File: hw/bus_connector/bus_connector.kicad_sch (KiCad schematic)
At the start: 11 parts, among them J1 DB9_Top, J2 DB9_Left, J3 DB9_Right

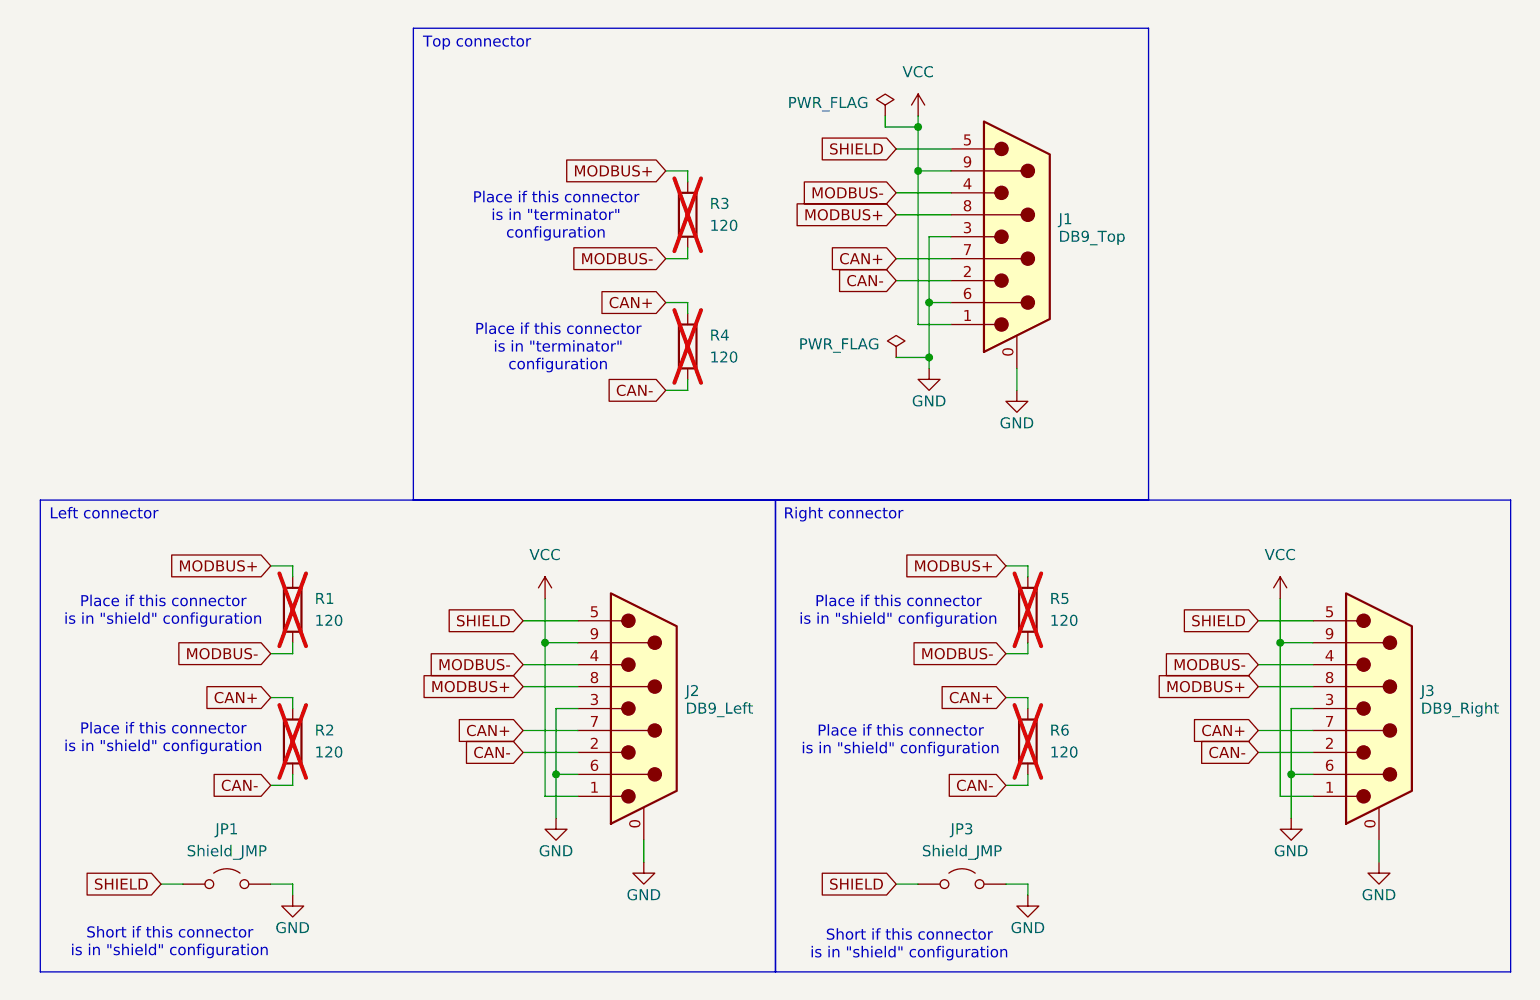
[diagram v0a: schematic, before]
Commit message: Add test layout to connector PCB
Signed-off-by: Mateusz Pająk <22417805+Tai-Min@users.noreply.github.com>
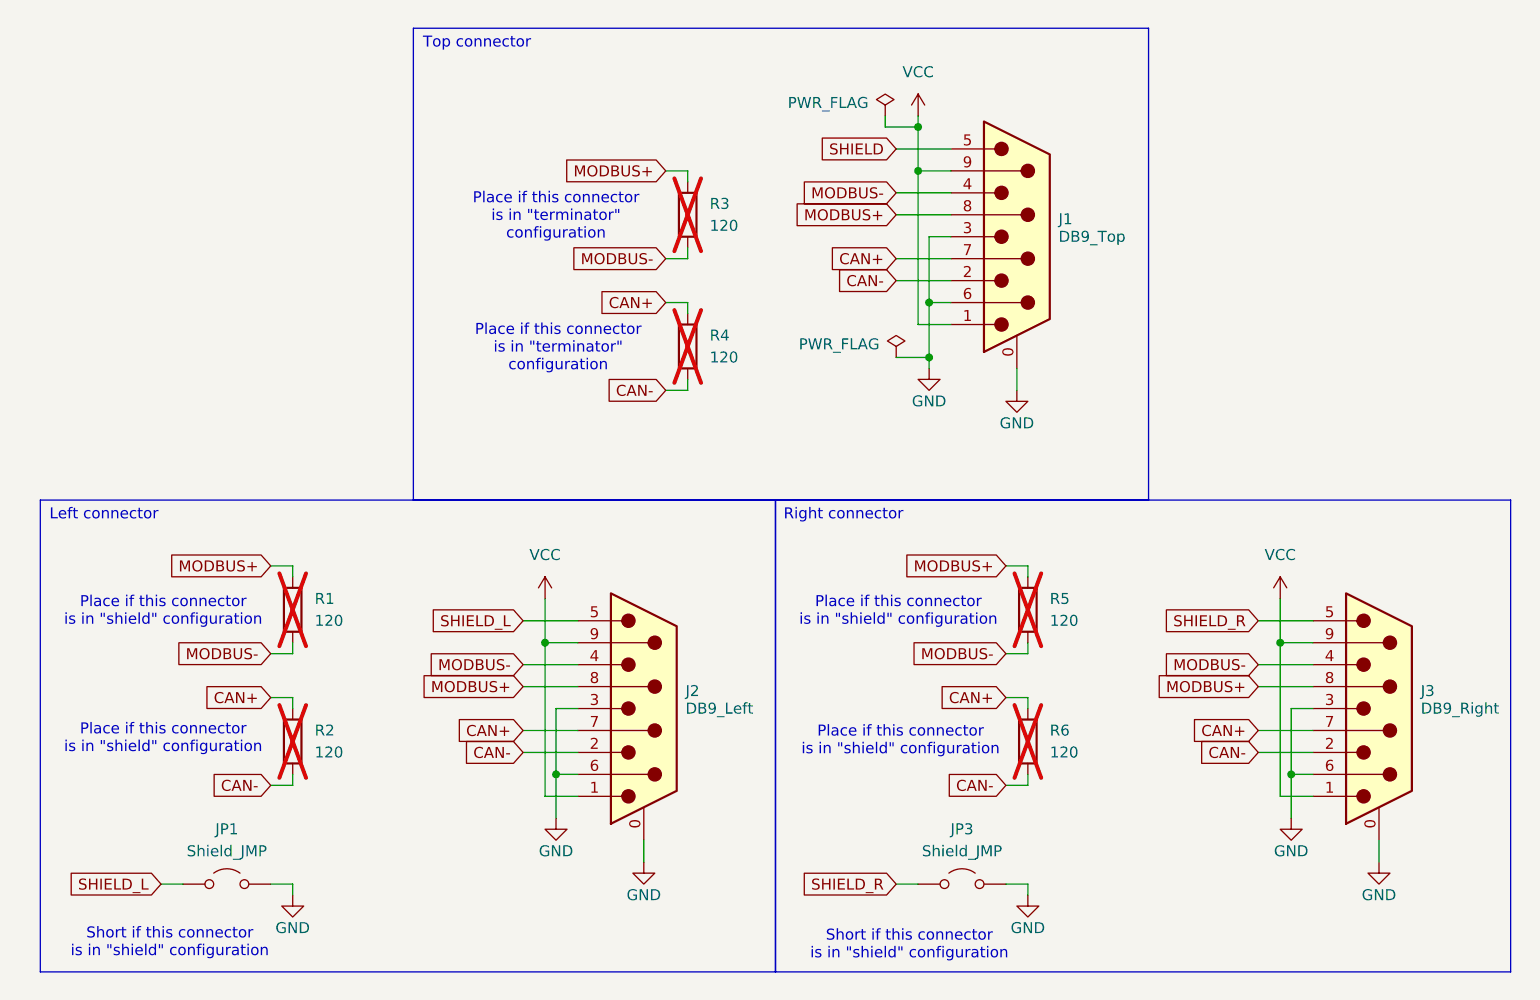
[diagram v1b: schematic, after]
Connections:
- net SHIELD: no longer J2.5, J3.5, JP1.1 (A), JP3.1 (A)
- new net SHIELD_L: J2.5, JP1.1 (A)
- new net SHIELD_R: J3.5, JP3.1 (A)
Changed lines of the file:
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@@
+		)
+	)
+	(global_label "SHIELD_R"
+		(shape input)
+		(at 205.74 104.14 180)
+		(fields_autoplaced yes)
+		(effects
+			(font
+				(size 1.27 1.27)
+			)
+			(justify right)
+		)
+		(property "Intersheetrefs" "${INTERSHEET_REFS}"
+			(at 193.9253 104.14 0)
+			(effects
+				(font
+					(size 1.27 1.27)
+				)
+				(justify right)
+				(hide yes)
+			)
+		)
+	)
+	(global_label "MODBUS-"
+		(shape input)
+		(at 205.74 109.22 180)
+		(fields_autoplaced yes)
+		(effects
+			(font
+				(size 1.27 1.27)
+			)
+			(justify right)
+		)
+		(property "Intersheetrefs" "${INTERSHEET_REFS}"
+			(at 193.3205 109.22 0)
+			(effects
+				(font
+					(size 1.27 1.27)
+				)
+				(justify right)
+				(hide yes)
+			)
 		)
 	)
 	(global_label "SHIELD"
 		(shape input)
-		(at 205.74 104.14 180)
-		(fields_autoplaced yes)
-		(effects
-			(font
-				(size 1.27 1.27)
-			)
-			(justify right)
-		)
-		(property "Intersheetrefs" "${INTERSHEET_REFS}"
-			(at 196.1629 104.14 0)
-			(effects
-				(font
-					(size 1.27 1.27)
-				)
-				(justify right)
-				(hide yes)
-			)
-		)
-	)
-	(global_label "MODBUS-"
-		(shape input)
-		(at 205.74 109.22 180)
-		(fields_autoplaced yes)
-		(effects
-			(font
-				(size 1.27 1.27)
-			)
-			(justify right)
-		)
-		(property "Intersheetrefs" "${INTERSHEET_REFS}"
-			(at 193.3205 109.22 0)
-			(effects
-				(font
-					(size 1.27 1.27)
-				)
-				(justify right)
-				(hide yes)
-			)
-		)
-	)
-	(global_label "SHIELD"
-		(shape input)
 		(at 163.83 49.53 180)
 		(fields_autoplaced yes)
@@
 		)
 	)
-	(global_label "SHIELD"
+	(global_label "SHIELD_R"
 		(shape input)
 		(at 163.83 134.62 180)
@@
 		)
 		(property "Intersheetrefs" "${INTERSHEET_REFS}"
-			(at 154.2529 134.62 0)
+			(at 152.0153 134.62 0)
 			(effects
 				(font
@@
 		)
 	)
-	(global_label "SHIELD"
+	(global_label "SHIELD_L"
 		(shape input)
 		(at 120.65 104.14 180)
@@
 		)
 		(property "Intersheetrefs" "${INTERSHEET_REFS}"
-			(at 111.0729 104.14 0)
+			(at 109.0772 104.14 0)
 			(effects
 				(font
@@
 		)
 	)
-	(global_label "SHIELD"
+	(global_label "SHIELD_L"
 		(shape input)
 		(at 78.74 134.62 180)
@@
 		)
 		(property "Intersheetrefs" "${INTERSHEET_REFS}"
-			(at 69.1629 134.62 0)
-			(effects
-				(font
+			(at 67.1672 134.62 0)
+			(effects
+				(font

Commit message: Edit actions
Signed-off-by: Mateusz Pająk <22417805+Tai-Min@users.noreply.github.com>
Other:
- moved on the sheet: J1, J2, J3, JP1, JP3, R1, R2, R3, R4, R5, R6

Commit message: Fix issues with bus connector project
Signed-off-by: Mateusz Pająk <22417805+Tai-Min@users.noreply.github.com>
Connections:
- net SHIELD: no longer names the net of J1.5
- no-connect marks 0 -> 1
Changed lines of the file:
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@@
 		(color 0 0 0 0)
 	)
+	(no_connect
+		(at 170.18 50.8)
+	)
 	(wire
 		(pts
@@
 		(pts
 			(xy 139.7 68.58) (xy 137.16 68.58)
-		)
-		(stroke
-			(width 0)
-			(type default)
-		)
-	)
-	(wire
-		(pts
-			(xy 163.83 50.8) (xy 170.18 50.8)
 		)
 		(stroke
@@
 			(effects
 				(font
-					(size 1.27 1.27)
-				)
-				(justify right)
-				(hide yes)
-			)
-		)
-	)
-	(global_label "SHIELD"
-		(shape input)
-		(at 163.83 50.8 180)
-		(fields_autoplaced yes)
-		(effects
-			(font
-				(size 1.27 1.27)
-			)
-			(justify right)
-		)
-		(property "Intersheetrefs" "${INTERSHEET_REFS}"
-			(at 154.2529 50.8 0)
-			(effects
-				(font

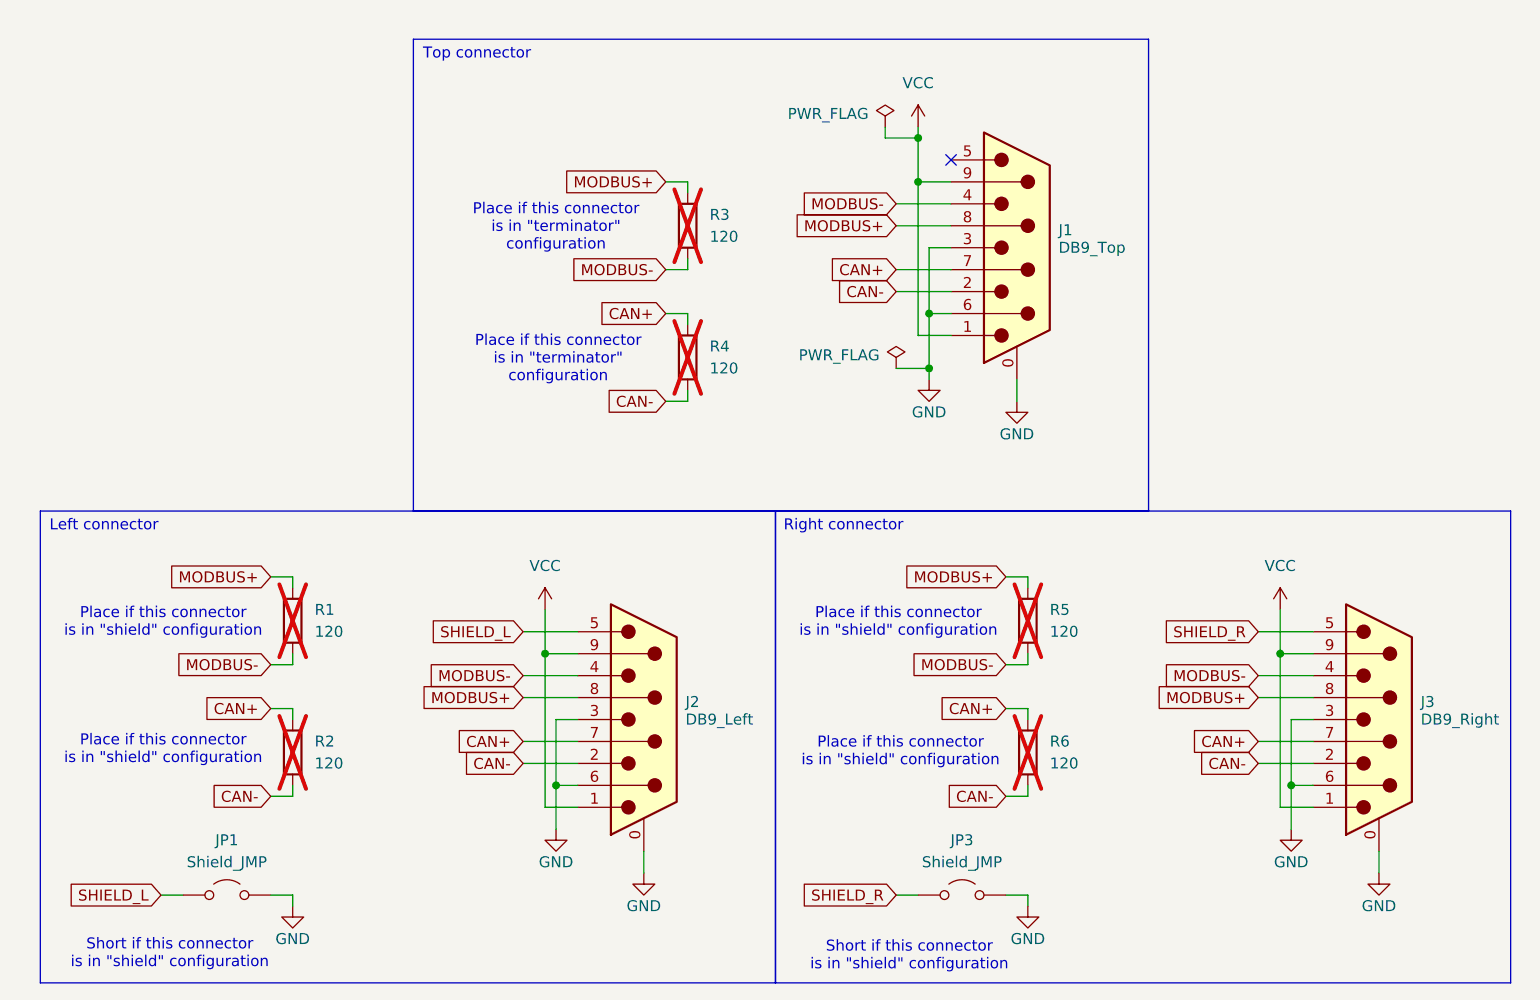
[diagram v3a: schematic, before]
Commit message: Fix bus connector errors
Signed-off-by: Mateusz Pająk <22417805+Tai-Min@users.noreply.github.com>
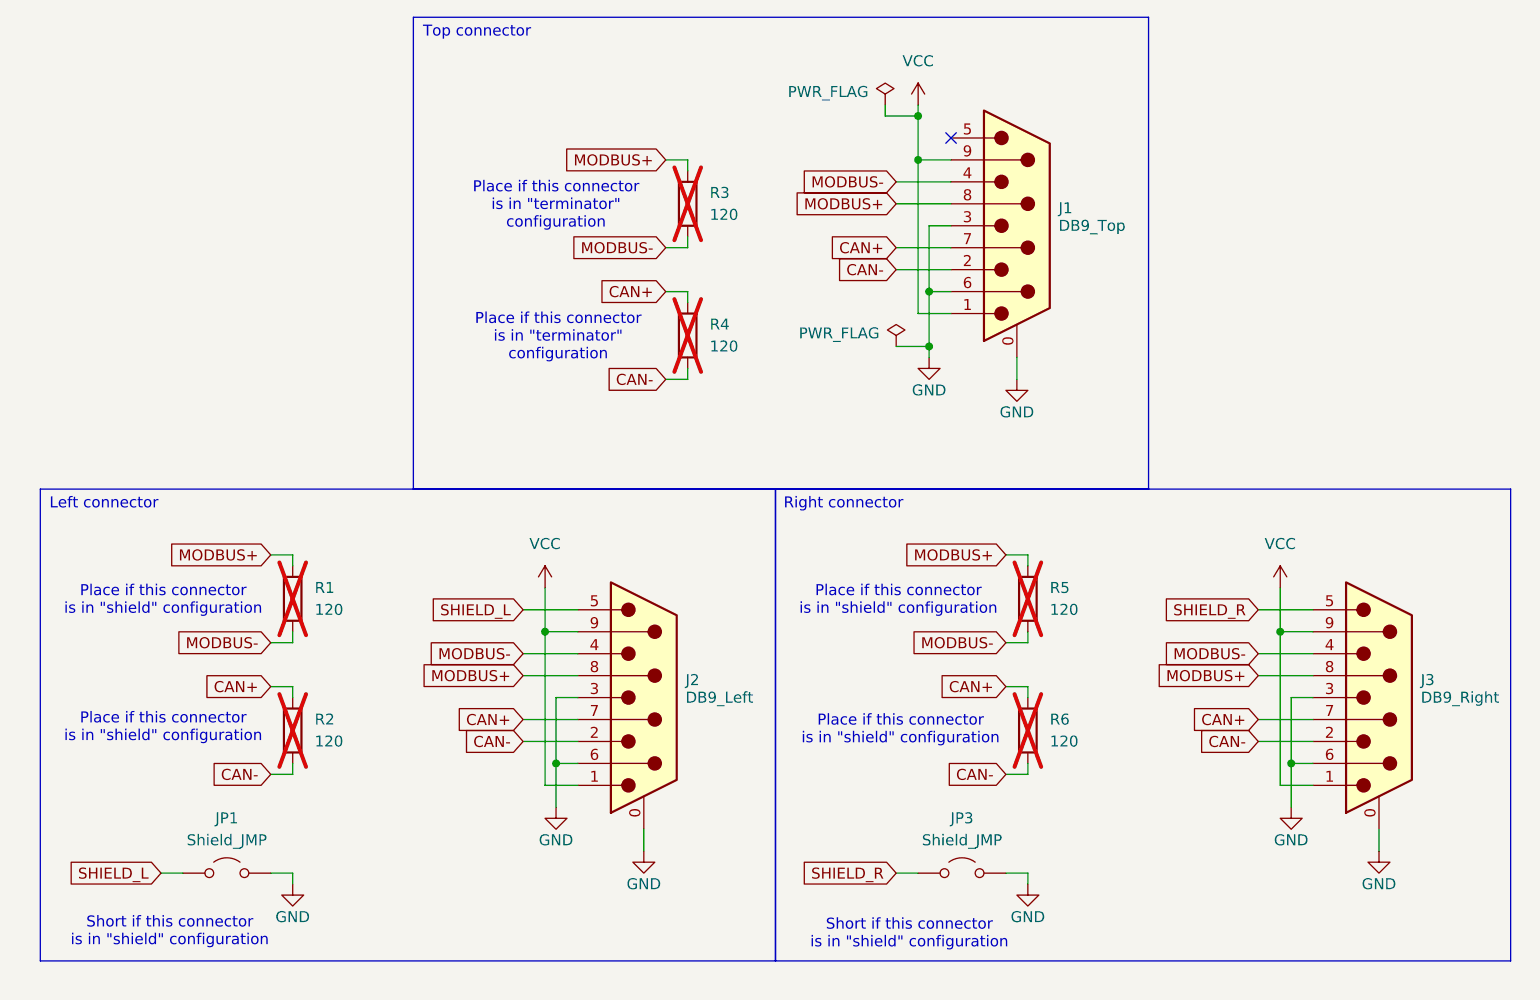
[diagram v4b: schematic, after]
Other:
- moved on the sheet: J1, J2, J3, JP1, JP3, R1, R2, R3, R4, R5, R6

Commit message: Finish connector prototype
Signed-off-by: Mateusz Pająk <22417805+Tai-Min@users.noreply.github.com>
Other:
- moved on the sheet: J1, J2, J3, JP1, JP3, R1, R2, R3, R4, R5, R6
